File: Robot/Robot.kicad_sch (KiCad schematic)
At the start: 1 part

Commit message: Update Robot SCH
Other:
- sheet FPGA ports: added DLED, PWR_OFF; removed none
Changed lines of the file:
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@@
+			)
+		)
+		(pin "DLED" output
+			(at 138.43 73.66 0)
+			(effects
+				(font
+					(size 1.27 1.27)
+				)
+				(justify right)
+			)
+		)
+		(pin "PWR_OFF" output
+			(at 138.43 76.2 0)
+			(effects
+				(font
+					(size 1.27 1.27)
+				)
+				(justify right)
 			)
 		)

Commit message: Updated Robot SCH
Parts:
- added C27: 1.0, symbol Device:C
- added J1: Lidar, symbol Connector:Conn_01x05_Pin
- added J10: Servo1, symbol Connector:Conn_01x03_Pin
- added J11: Servo2, symbol Connector:Conn_01x03_Pin
- added J12: Servo3, symbol Connector:Conn_01x03_Pin
- added J13: Servo4, symbol Connector:Conn_01x03_Pin
- added J14: Servo5, symbol Connector:Conn_01x03_Pin
- added J15: Servo6, symbol Connector:Conn_01x03_Pin
- added J16: Servo7, symbol Connector:Conn_01x03_Pin
- added J2: Console, symbol Connector:Conn_01x04_Pin
- added R24, R25: 5K1, symbol Device:R
- added R5: 10K, Resistor_SMD:R_0603_1608Metric_Pad0.98x0.95mm_HandSolder, symbol Device:R
- added U5: ADC128D818, Package_SO:TSSOP-16_4.4x5mm_P0.65mm, symbol Analog_ADC:ADC128D818
- U1: value ~ -> MaixCAM2
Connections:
- net FPGA/DL_CRESET: now also R5.2
- net FPGA/SCL: now also R25.2, U5.3 (SCL)
- net FPGA/SDA: now also R24.2, U5.2 (SDA)
- net FPGA/SERV1: now also J10.3 (Pin_3)
- net FPGA/SERV2: now also J11.3 (Pin_3)
- net FPGA/SERV3: now also J12.3 (Pin_3)
- net FPGA/SERV4: now also J13.3 (Pin_3)
- net FPGA/SERV5: now also J14.3 (Pin_3)
- net LIDAR_TX: now also J1.1 (Pin_1)
- net GND: now reaches U1.1 (GND)
- net GND: now also U1.1 (GND), U1.7 (GND), C27.1, J1.4 (Pin_4), J10.1 (Pin_1), J11.1 (Pin_1), J12.1 (Pin_1), J13.1 (Pin_1), J14.1 (Pin_1), J15.1 (Pin_1), J16.1 (Pin_1), J2.4 (Pin_4), R5.1, U5.4 (GND), U5.7 (A0), U5.8 (A1)
- net +5V: now reaches U1.2 (5V)
- net +5V: now also J1.5 (Pin_5)
- net at U1.11 (A28/UART0_TX): now also J2.2 (Pin_2)
- net at U1.5 (A29/UART0_RX): now also J2.3 (Pin_3)
- net LIDAR_RX renamed INT
- net INT: now also U5.6 (~{INT})
- new net +3.3V: C27.2, J2.1 (Pin_1), R24.1, R25.1, U5.5 (V+)
- new net FPGA/SERV6: J15.3 (Pin_3)
- new net FPGA/SERV7: J16.3 (Pin_3)
- new net Pots/O1: U5.11 (IN5)
- new net Pots/O2: U5.10 (IN6)
- new net Pots/O3: U5.9 (IN7)
- new net Pots/Ref: U5.12 (IN4)
- new net Power/Pwr1: J10.2 (Pin_2), J11.2 (Pin_2), J12.2 (Pin_2), J13.2 (Pin_2)
- new net Power/Pwr2: J14.2 (Pin_2), J15.2 (Pin_2), J16.2 (Pin_2)
- new net S12: U5.15 (IN1)
- new net S5: U5.16 (IN0)
- new net SP1: U5.14 (IN2)
- new net SP2: U5.13 (IN3)
- no-connect marks 0 -> 3
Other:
- added sheet Pots (pots.kicad_sch)
- added sheet Power (power.kicad_sch)
- sheet FPGA ports: added PwrBtnInput, SERV6, SERV7; removed none
- moved on the sheet: U1A, U1B

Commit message: Updated Robot SCH
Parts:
- added J17: Beacon, symbol Connector:Conn_01x04_Pin
- added J3: DLED, symbol Connector:Conn_01x03_Socket
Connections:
- net +3.3V: now also J17.1 (Pin_1)
- net FPGA/DLED: now also J3.2 (Pin_2)
- net FPGA/SCL: now also J17.3 (Pin_3)
- net FPGA/SDA: now also J17.2 (Pin_2)
- net GND: now also J17.4 (Pin_4), J3.3 (Pin_3)
- net Power/Pwr2: now also J3.1 (Pin_1)

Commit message: Started PCB roughting
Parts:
- added H1, H2, H3, H4, H5, H6: MountingHole, MountingHole:MountingHole_2.5mm, symbol Mechanical:MountingHole
- C1: renamed from C27; footprint (none) -> Capacitor_SMD:C_0603_1608Metric_Pad1.08x0.95mm_HandSolder
- J1: renamed from J10; footprint (none) -> Connector_PinHeader_2.54mm:PinHeader_1x03_P2.54mm_Vertical
- J10: renamed from J1; footprint (none) -> Connector_PinHeader_2.54mm:PinHeader_1x05_P2.54mm_Vertical
- J11: renamed from J2; footprint (none) -> Connector_PinHeader_2.54mm:PinHeader_1x04_P2.54mm_Vertical
- J2: renamed from J11; footprint (none) -> Connector_PinHeader_2.54mm:PinHeader_1x03_P2.54mm_Vertical
- J3: renamed from J12; footprint (none) -> Connector_PinHeader_2.54mm:PinHeader_1x03_P2.54mm_Vertical
- J4: renamed from J13; footprint (none) -> Connector_PinHeader_2.54mm:PinHeader_1x03_P2.54mm_Vertical
- J5: renamed from J14; footprint (none) -> Connector_PinHeader_2.54mm:PinHeader_1x03_P2.54mm_Vertical
- J6: renamed from J15; footprint (none) -> Connector_PinHeader_2.54mm:PinHeader_1x03_P2.54mm_Vertical
- J7: renamed from J16; footprint (none) -> Connector_PinHeader_2.54mm:PinHeader_1x03_P2.54mm_Vertical
- J8: renamed from J17; footprint (none) -> Connector_PinHeader_2.54mm:PinHeader_1x04_P2.54mm_Vertical
- J9: renamed from J3; footprint (none) -> Connector_PinHeader_2.54mm:PinHeader_1x03_P2.54mm_Horizontal
- R1: renamed from R24; footprint (none) -> Resistor_SMD:R_0603_1608Metric_Pad0.98x0.95mm_HandSolder
- R2: renamed from R25; footprint (none) -> Resistor_SMD:R_0603_1608Metric_Pad0.98x0.95mm_HandSolder
- U2: renamed from U1; footprint (none) -> easyeda2kicad:CONN-TH_18P-P2.54_B18B-XADSS-N-LF-SN
- renumbered R5 to R3, U5 to U1
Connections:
- net +5V: now also U2.14 (5V), U2.2 (5V), U2.8 (5V); no longer U2.2 (5V)
- net FPGA/DL_CDONE: now also U2.18 (UART4_RX); no longer U2.6 (UART4_RX)
- net FPGA/DL_CRESET: now also U2.17 (UART4_TX); no longer U2.5 (UART4_TX)
- net FPGA/DL_SI: now also U2.16 (SPI1_MOSI); no longer U2.4 (SPI1_MOSI)
- net FPGA/DL_SO: now also U2.15 (SPI1_MISO); no longer U2.3 (SPI1_MISO)
- net GND: now also U2.13 (GND); no longer U2.1 (GND)

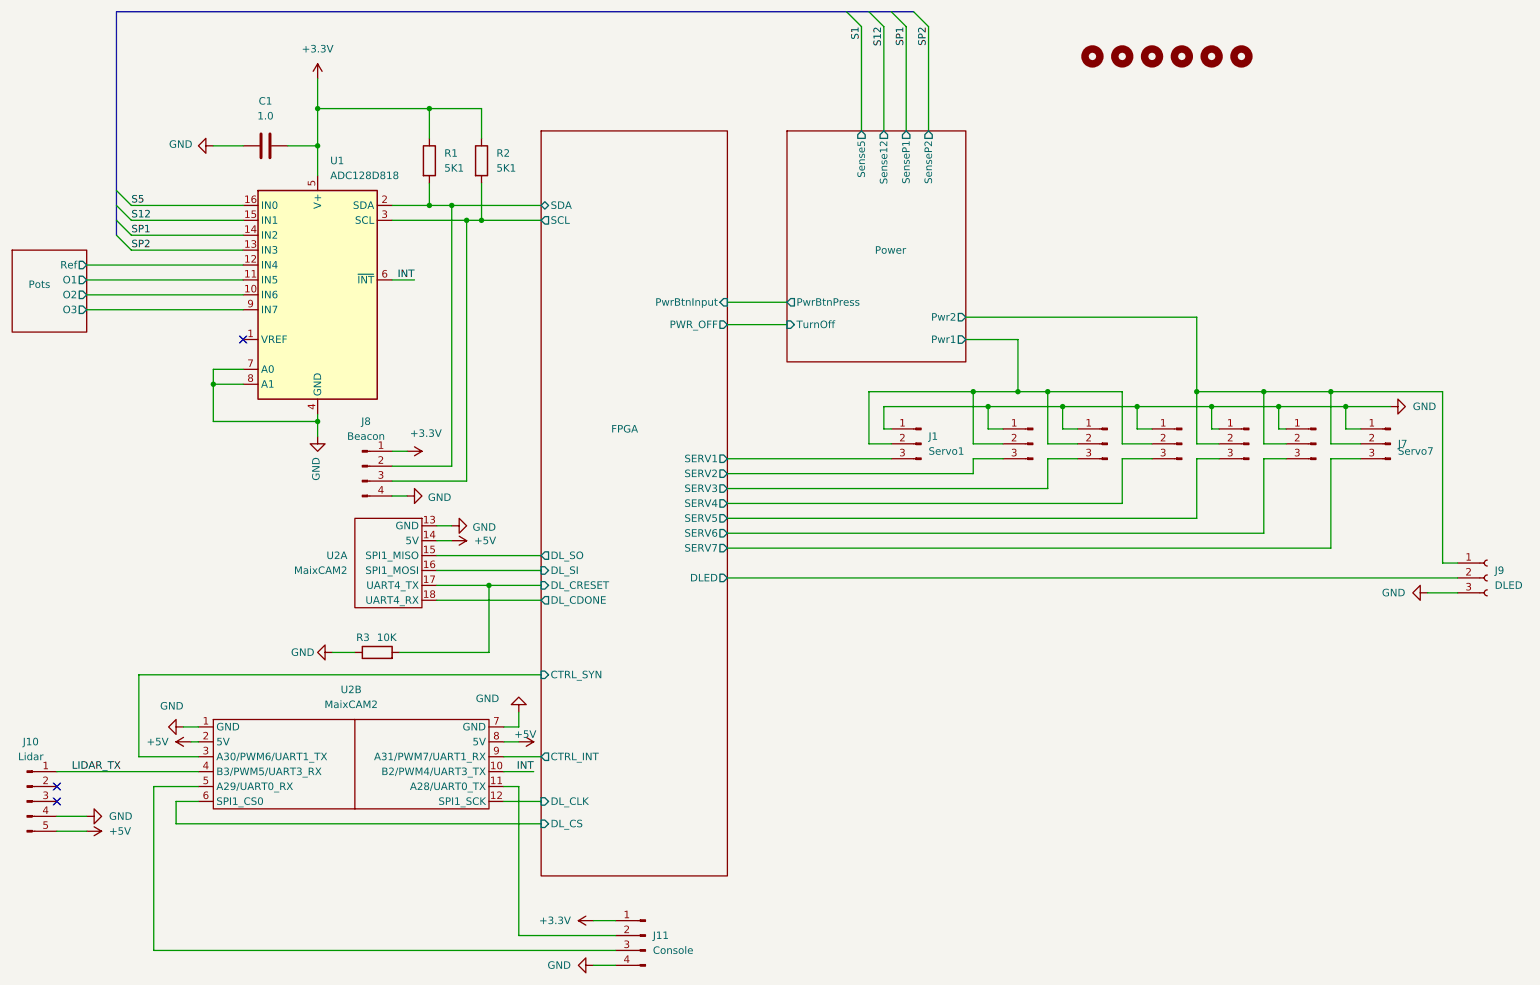
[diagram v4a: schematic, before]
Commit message: Updated SCH & PCB for Robot
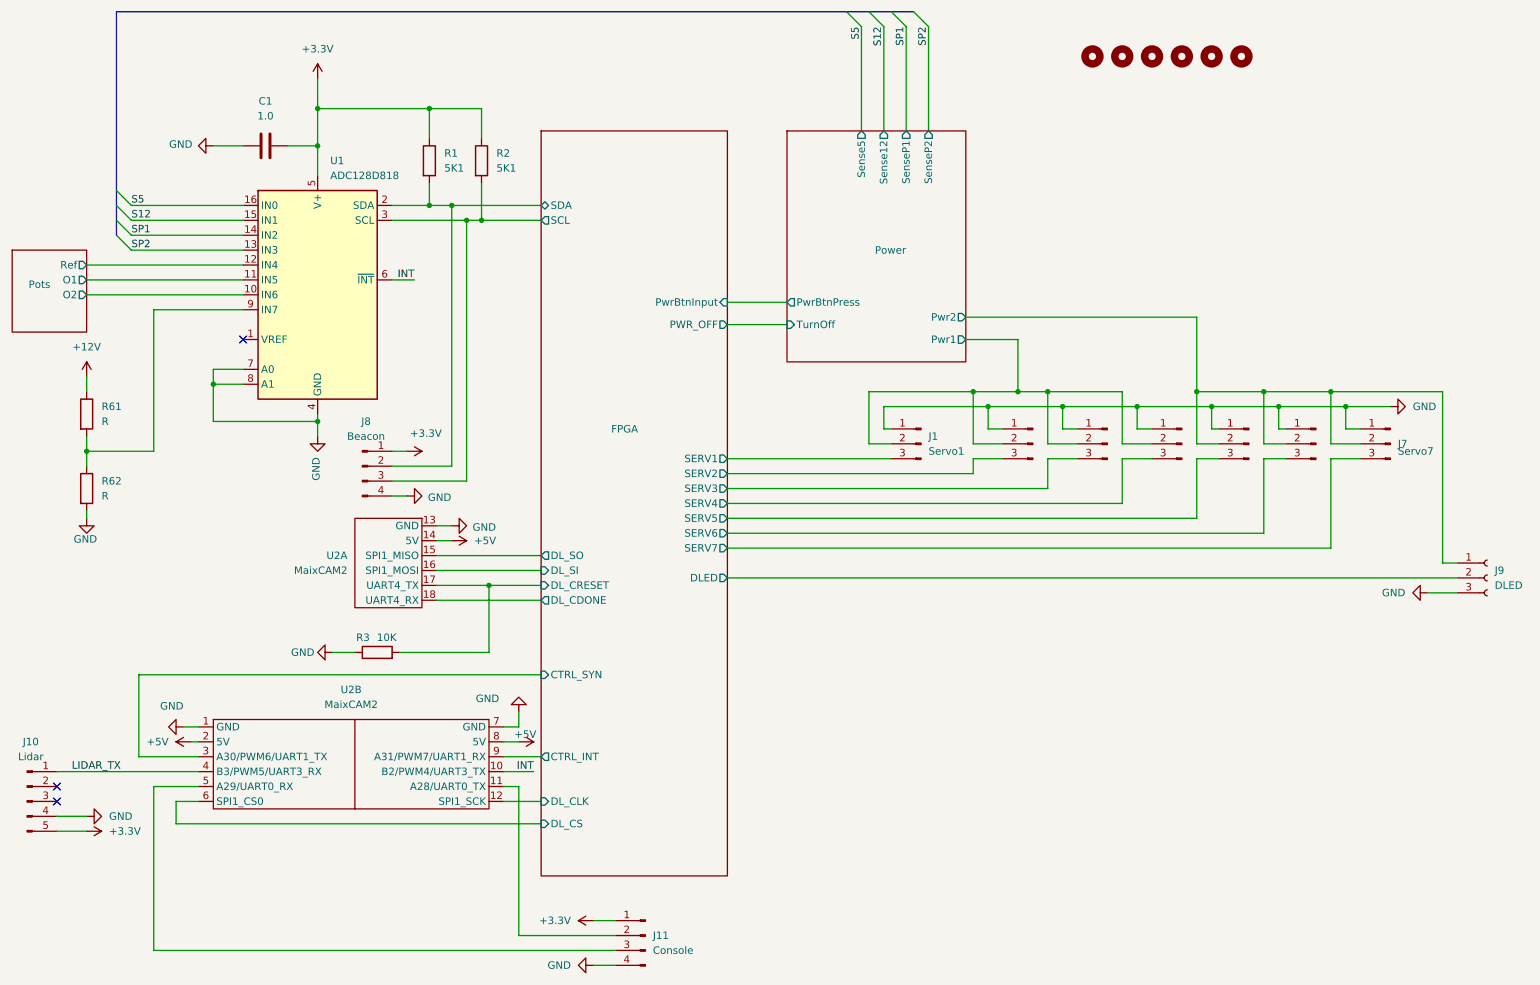
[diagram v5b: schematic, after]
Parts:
- added R61, R62: R, Resistor_SMD:R_0603_1608Metric_Pad0.98x0.95mm_HandSolder, symbol Device:R
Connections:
- net +3.3V: now also J10.5 (Pin_5)
- net +5V: no longer J10.5 (Pin_5)
- net GND: now also R62.2
- net Pots/O3: no longer names the net of U1.9 (IN7)
- net Pots/O3: now also R61.2, R62.1
- new net +12V: R61.1
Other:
- sheet Pots ports: added none; removed O3

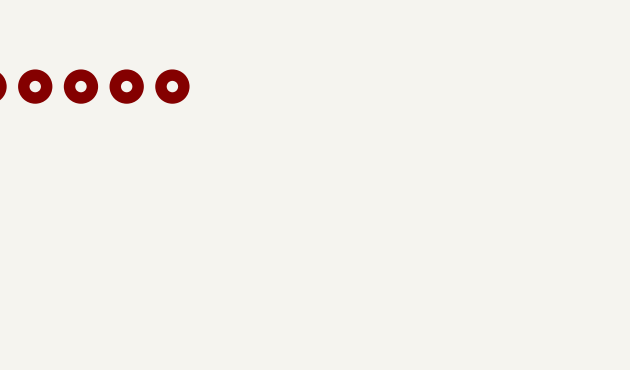
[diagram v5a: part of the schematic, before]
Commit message: Added MaixCAM stand on SCH & PCB
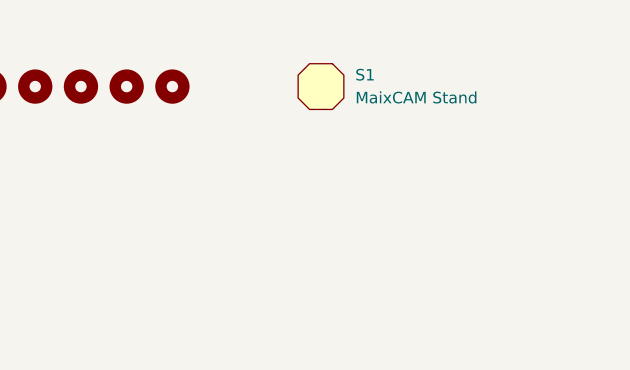
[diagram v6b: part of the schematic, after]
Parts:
- added S1: MaixCAM Stand, locals:Stand, symbol Mechanical:Mechanical_Shape
- J8: footprint Connector_PinHeader_2.54mm:PinHeader_1x04_P2.54mm_Vertical -> Connector_JST:JST_XH_B4B-XH-A_1x04_P2.50mm_Vertical
- J9: footprint Connector_PinHeader_2.54mm:PinHeader_1x03_P2.54mm_Horizontal -> easyeda2kicad:CONN-TH_S3B-XH-A-1-LF-SN
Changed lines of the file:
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@@
+	)
+	(symbol
+		(lib_id "Mechanical:Mechanical_Shape")
+		(at 242.57 25.4 0)
+		(unit 1)
+		(exclude_from_sim yes)
+		(in_bom no)
+		(on_board yes)
+		(dnp no)
+		(fields_autoplaced yes)
+		(property "Reference" "S1"
+			(at 246.38 24.1299 0)
+			(effects
+				(font
+					(size 1.27 1.27)
+				)
+				(justify left)
+			)
+		)
+		(property "Value" "MaixCAM Stand"
+			(at 246.38 26.6699 0)
+			(effects
+				(font
+					(size 1.27 1.27)
+				)
+				(justify left)
+			)
+		)
+		(property "Footprint" "locals:Stand"
+			(at 242.57 30.48 0)
+			(effects
+				(font
+					(size 1.27 1.27)
+				)
+				(hide yes)
+			)
+		)
+		(property "Datasheet" "~"
+			(at 242.57 21.59 0)
+			(effects
+				(font
+					(size 1.27 1.27)
+				)
+				(hide yes)
+			)
+		)
+		(property "Description" "Mechanical shape, non-electric, board outlines"
+			(at 242.57 25.4 0)
+			(effects
+				(font
+					(size 1.27 1.27)
+				)
+				(hide yes)
+			)
+		)
+		(instances
+			(project "Robot"
+				(path "/c5aa62e4-5f59-48a4-ae5d-57fc70429dc3"
+					(reference "S1")
+					(unit 1)
+				)
+			)
+		)
 	)
 	(symbol
@@
 			)
 		)
-		(property "Footprint" "Connector_PinHeader_2.54mm:PinHeader_1x03_P2.54mm_Horizontal"
+		(property "Footprint" "easyeda2kicad:CONN-TH_S3B-XH-A-1-LF-SN"
 			(at 267.97 114.3 0)
 			(effects
@@
 			)
 		)
-		(property "Footprint" "Connector_PinHeader_2.54mm:PinHeader_1x04_P2.54mm_Vertical"
+		(property "Footprint" "Connector_JST:JST_XH_B4B-XH-A_1x04_P2.50mm_Vertical"
 			(at 76.2 95.25 0)
 			(effects

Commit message: Updated PCB & Patterns for Robot
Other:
- company: (none) -> RoboWay
- title: (none) -> Main
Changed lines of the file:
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@@
 	(generator_version "9.0")
 	(paper "A4")
+	(title_block
+		(title "Main")
+		(company "RoboWay")
+	)
 	(junction
 		(at 187.96 82.55)

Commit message: Updated PCB for Robot (routing in progress)
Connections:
- net Power/Pwr1: now also J9.1 (Pin_1); no longer J4.2 (Pin_2)
- net Power/Pwr2: now also J4.2 (Pin_2); no longer J9.1 (Pin_1)
